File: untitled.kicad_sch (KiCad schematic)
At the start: 22 parts, among them IC28 INA226AIDGSR, IC29 TPS25940ARVCR

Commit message: Some edits
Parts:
- R_ILIM: value 24k -> 16.9k
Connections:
- net 3.3V: now also C78.1, IC28.6 (VS), R37.2, R38.2
- net SDA2: now also R_ADD_CONFIG1.1
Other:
- moved on the sheet: R37, R38, R_ADD_CONFIG1

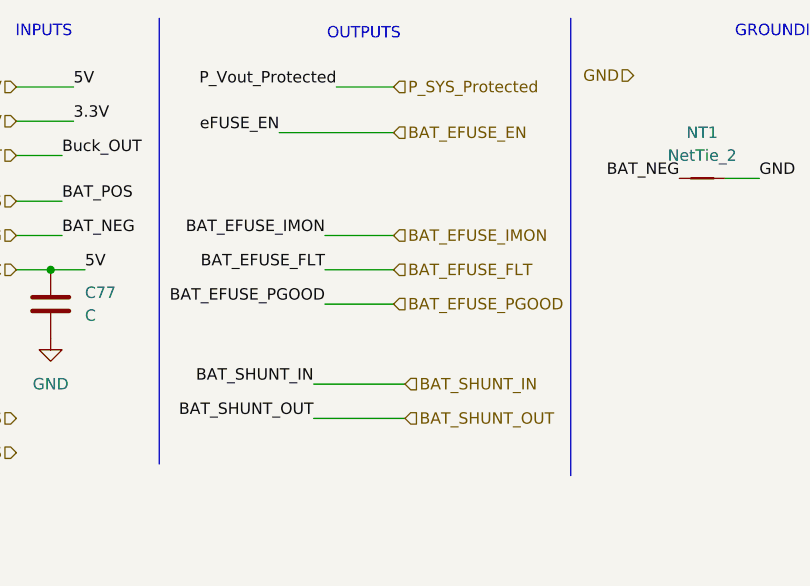
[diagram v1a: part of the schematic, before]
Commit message: Modification of ROOT sheet blocks
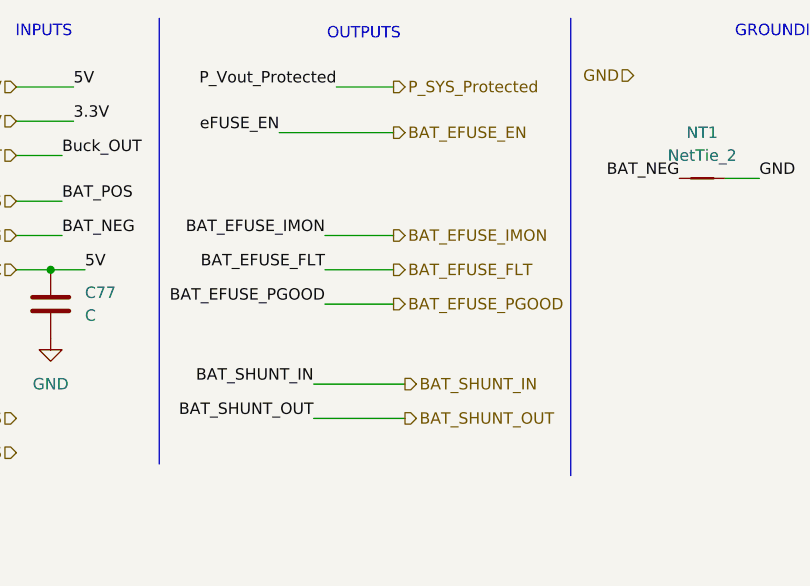
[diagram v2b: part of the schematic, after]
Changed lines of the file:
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@@
 	)
 	(hierarchical_label "BAT_SHUNT_IN"
-		(shape input)
+		(shape output)
 		(at 72.39 54.61 0)
 		(effects
@@
 	)
 	(hierarchical_label "BAT_EFUSE_IMON"
-		(shape input)
+		(shape output)
 		(at 71.12 38.1 0)
 		(effects
@@
 	)
 	(hierarchical_label "BAT_EFUSE_EN"
-		(shape input)
+		(shape output)
 		(at 71.12 26.67 0)
 		(effects
@@
 	)
 	(hierarchical_label "BAT_SHUNT_OUT"
-		(shape input)
+		(shape output)
 		(at 72.39 58.42 0)
 		(effects
@@
 	)
 	(hierarchical_label "BAT_EFUSE_FLT"
-		(shape input)
+		(shape output)
 		(at 71.12 41.91 0)
 		(effects
@@
 	)
 	(hierarchical_label "P_SYS_Protected"
-		(shape input)
+		(shape output)
 		(at 71.12 21.59 0)
 		(effects
@@
 	)
 	(hierarchical_label "BAT_EFUSE_PGOOD"
-		(shape input)
+		(shape output)
 		(at 71.12 45.72 0)
 		(effects

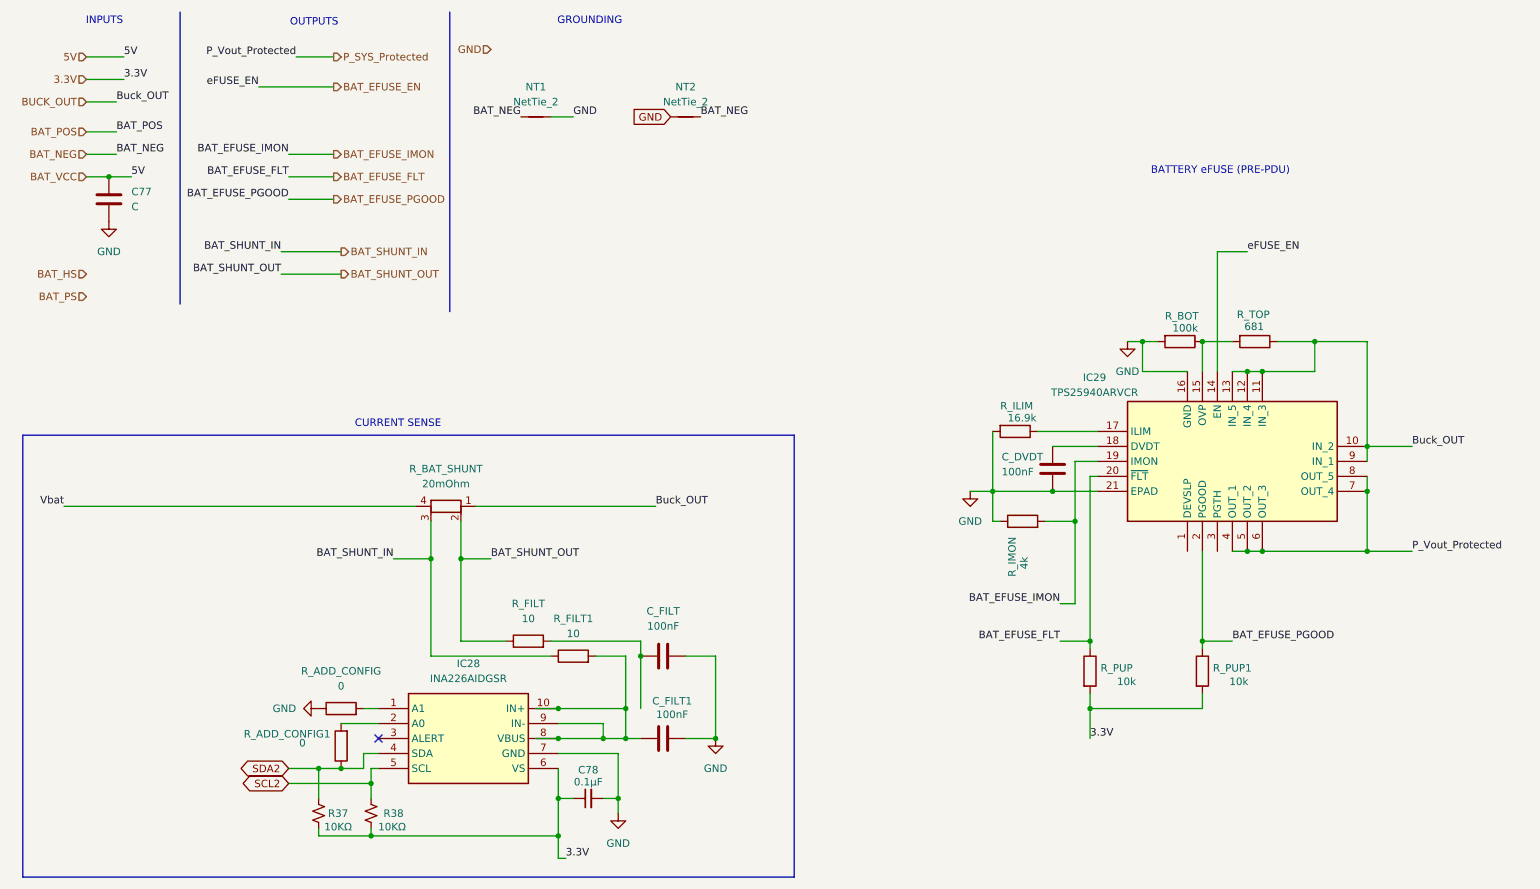
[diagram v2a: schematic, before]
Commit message: Adjusting footprints of components
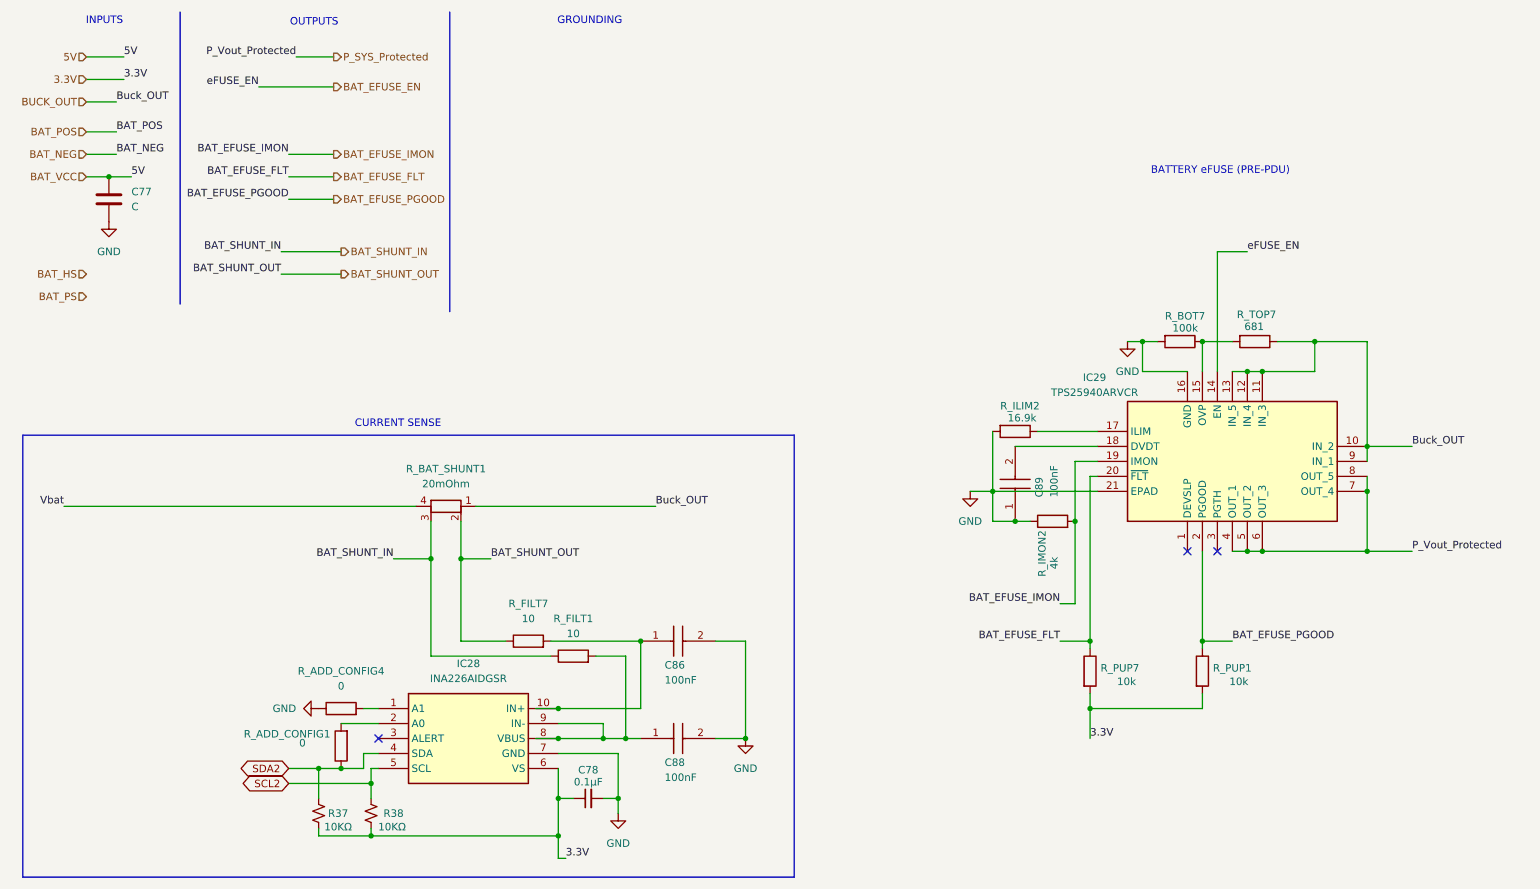
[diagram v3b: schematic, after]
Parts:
- removed C_DVDT, C_FILT, C_FILT1: 100nF, symbol Device:C
- removed NT1, NT2: NetTie_2, symbol Device:NetTie_2
- added C86, C88, C89: 100nF, C0603_Commercial, symbol PULSE_Library:C0603X6S0J104M030BC
- C78: footprint C0603 -> PULSE_Library:C0603
- IC28: footprint SOP50P490X110-10N -> PULSE_Library:SOP50P490X110-10N
- R37, R38: footprint RESC1608X55N -> PULSE_Library:RESC1608X55N
- R_ADD_CONFIG1, R_FILT1, R_PUP1: footprint (none) -> Resistor_SMD:R_0603_1608Metric
- R_ADD_CONFIG4: renamed from R_ADD_CONFIG; footprint (none) -> Resistor_SMD:R_0603_1608Metric
- R_BOT7: renamed from R_BOT; footprint (none) -> Resistor_SMD:R_0603_1608Metric
- R_FILT7: renamed from R_FILT; footprint (none) -> Resistor_SMD:R_0603_1608Metric
- R_ILIM2: renamed from R_ILIM; footprint (none) -> Resistor_SMD:R_0603_1608Metric
- R_IMON2: renamed from R_IMON; footprint (none) -> Resistor_SMD:R_0603_1608Metric
- R_PUP7: renamed from R_PUP; footprint (none) -> Resistor_SMD:R_0603_1608Metric
- R_TOP7: renamed from R_TOP; footprint (none) -> Resistor_SMD:R_0603_1608Metric
- renumbered R_BAT_SHUNT to R_BAT_SHUNT1
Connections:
- net GND: now also C86.2, C88.2, C89.1
- net at IC28.8 (VBUS), IC28.9 (IN-), R_FILT1.2: now also C88.1; no longer IC28.10 (IN+)
- net at IC29.18 (DVDT): now also C89.2
- net at R_FILT7.2: now also IC28.10 (IN+), C86.1
- no-connect marks 1 -> 3
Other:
- moved on the sheet: R_IMON2

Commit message: Big final PCU PCB design
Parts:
- added R_BYPASS14: 0, Resistor_SMD:R_0603_1608Metric, symbol Device:R
- added TP24: eFUSE_EN, TestPoint:TestPoint_Pad_D2.0mm, symbol Connector:TestPoint_Probe
- added TP25: Buck_out, TestPoint:TestPoint_Pad_D2.0mm, symbol Connector:TestPoint_Probe
- added TP27: eFUSE_OVP, TestPoint:TestPoint_Pad_D2.0mm, symbol Connector:TestPoint_Probe
- C77: footprint (none) -> Capacitor_SMD:C_0201_0603Metric
- C86, C88, C89: footprint C0603_Commercial -> Capacitor_SMD:C_0603_1608Metric
- R_BAT_SHUNT1: footprint (none) -> Resistor_SMD:R_Shunt_Vishay_WSKW0612
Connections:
- net Vbat is gone; now on net BAT_POS: R_BAT_SHUNT1.4
- net BAT_EFUSE_EN: now also TP24.1
- net BUCK_OUT: now also R_BYPASS14.1, TP25.1
- net P_SYS_Protected: now also R_BYPASS14.2
- net at IC29.15 (OVP), R_BOT7.1, R_TOP7.2: now also TP27.1
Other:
- moved on the sheet: C77, C78, C86, C88, C89, IC28, IC29, R37, R38, R_ADD_CONFIG1, R_ADD_CONFIG4, R_BAT_SHUNT1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
